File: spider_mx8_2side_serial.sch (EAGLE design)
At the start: 7 parts, among them J1 AVR_SPI_PRG_6NS

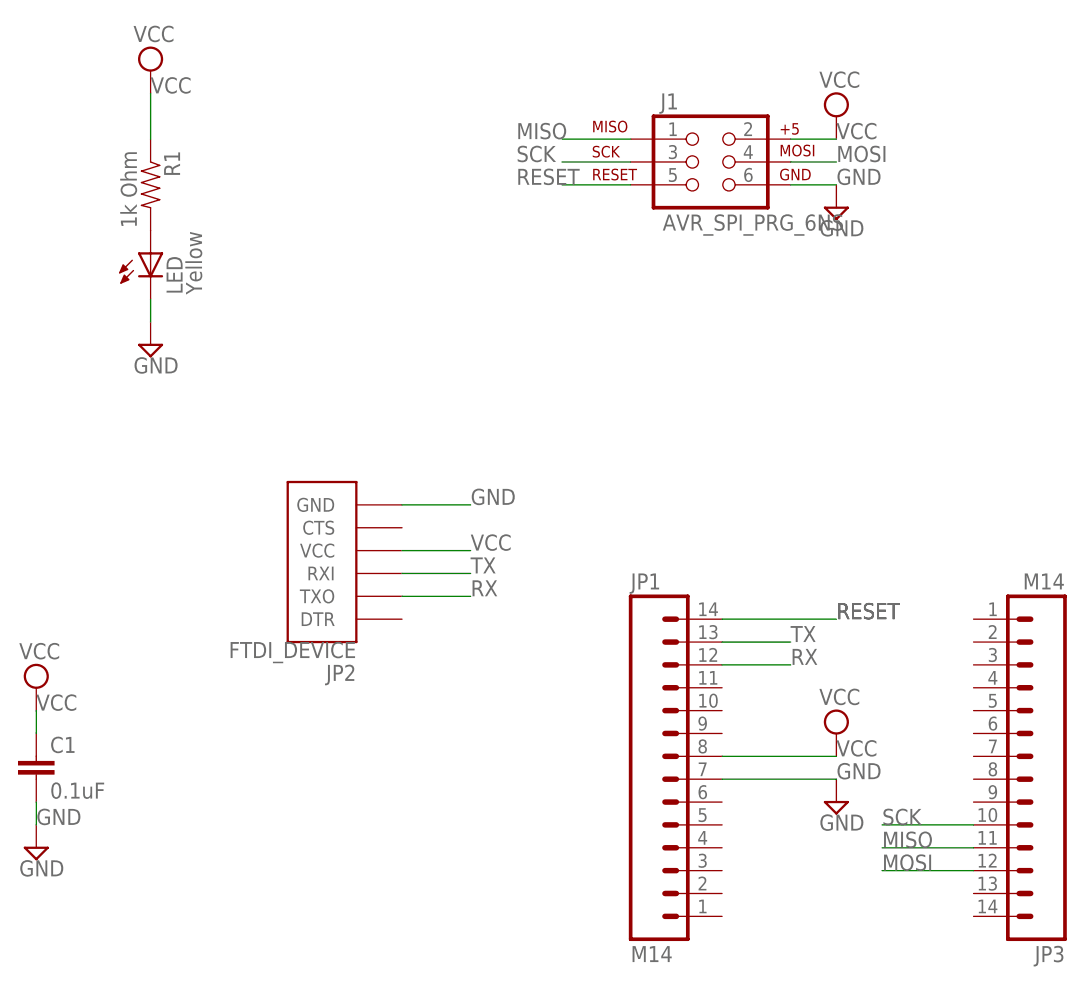
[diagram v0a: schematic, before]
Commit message: added power jumper to serial: mx8 spider
other tweaks include stuff with the 8LED modules
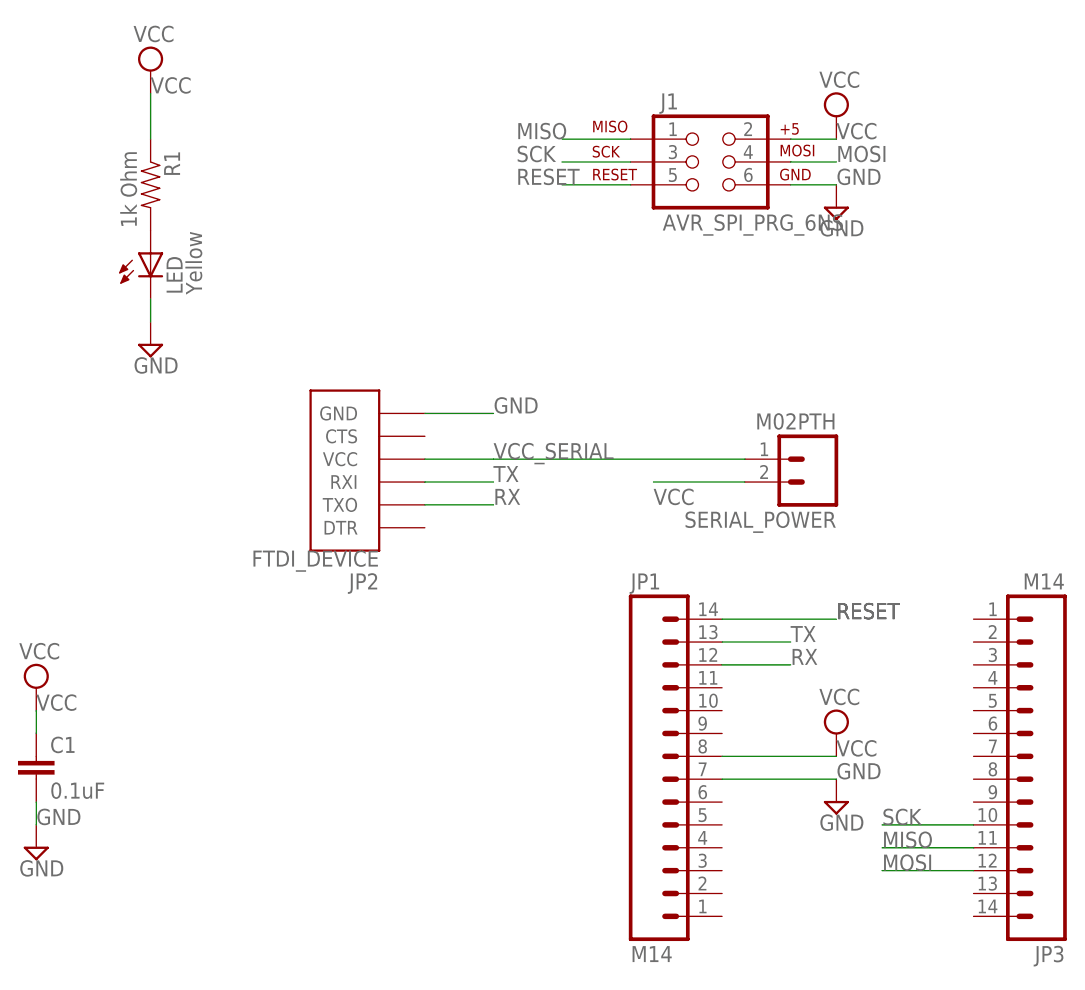
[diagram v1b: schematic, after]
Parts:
- added SERIAL_POWER: M02PTH, SparkFun-Connectors:M02PTH
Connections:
- new net VCC_SERIAL: JP2.VCC, SERIAL_POWER.1
- net VCC: now also SERIAL_POWER.2; no longer JP2.VCC
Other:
- moved on the sheet: JP2
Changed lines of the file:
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@@
 <grid distance="0.1" unitdist="inch" unit="inch" style="lines" multiple="1" display="no" altdistance="0.01" altunitdist="inch" altunit="inch"/>
 <layers>
-<layer number="1" name="Top" color="4" fill="1" visible="yes" active="no"/>
-<layer number="16" name="Bottom" color="1" fill="1" visible="yes" active="no"/>
-<layer number="17" name="Pads" color="2" fill="1" visible="yes" active="no"/>
-<layer number="18" name="Vias" color="2" fill="1" visible="yes" active="no"/>
-<layer number="19" name="Unrouted" color="6" fill="1" visible="yes" active="no"/>
-<layer number="20" name="Dimension" color="15" fill="1" visible="yes" active="no"/>
-<layer number="21" name="tPlace" color="7" fill="1" visible="yes" active="no"/>
-<layer number="22" name="bPlace" color="7" fill="1" visible="yes" active="no"/>
-<layer number="23" name="tOrigins" color="15" fill="1" visible="yes" active="no"/>
-<layer number="24" name="bOrigins" color="15" fill="1" visible="yes" active="no"/>
-<layer number="25" name="tNames" color="7" fill="1" visible="yes" active="no"/>
-<layer number="26" name="bNames" color="7" fill="1" visible="yes" active="no"/>
-<layer number="27" name="tValues" color="7" fill="1" visible="yes" active="no"/>
-<layer number="28" name="bValues" color="7" fill="1" visible="yes" active="no"/>
+<layer number="1" name="Top" color="4" fill="1" visible="no" active="no"/>
+<layer number="16" name="Bottom" color="1" fill="1" visible="no" active="no"/>
+<layer number="17" name="Pads" color="2" fill="1" visible="no" active="no"/>
+<layer number="18" name="Vias" color="2" fill="1" visible="no" active="no"/>
+<layer number="19" name="Unrouted" color="6" fill="1" visible="no" active="no"/>
+<layer number="20" name="Dimension" color="15" fill="1" visible="no" active="no"/>
+<layer number="21" name="tPlace" color="7" fill="1" visible="no" active="no"/>
+<layer number="22" name="bPlace" color="7" fill="1" visible="no" active="no"/>
+<layer number="23" name="tOrigins" color="15" fill="1" visible="no" active="no"/>
+<layer number="24" name="bOrigins" color="15" fill="1" visible="no" active="no"/>
+<layer number="25" name="tNames" color="7" fill="1" visible="no" active="no"/>
+<layer number="26" name="bNames" color="7" fill="1" visible="no" active="no"/>
+<layer number="27" name="tValues" color="7" fill="1" visible="no" active="no"/>
+<layer number="28" name="bValues" color="7" fill="1" visible="no" active="no"/>
 <layer number="29" name="tStop" color="7" fill="3" visible="no" active="no"/>
 <layer number="30" name="bStop" color="7" fill="6" visible="no" active="no"/>
@@
 <layer number="35" name="tGlue" color="7" fill="4" visible="no" active="no"/>
 <layer number="36" name="bGlue" color="7" fill="5" visible="no" active="no"/>
-<layer number="37" name="tTest" color="7" fill="1" visible="yes" active="no"/>
-<layer number="38" name="bTest" color="7" fill="1" visible="yes" active="no"/>
+<layer number="37" name="tTest" color="7" fill="1" visible="no" active="no"/>
+<layer number="38" name="bTest" color="7" fill="1" visible="no" active="no"/>
 <layer number="39" name="tKeepout" color="4" fill="11" visible="no" active="no"/>
 <layer number="40" name="bKeepout" color="1" fill="11" visible="no" active="no"/>
@@
 <layer number="44" name="Drills" color="7" fill="1" visible="no" active="no"/>
 <layer number="45" name="Holes" color="7" fill="1" visible="no" active="no"/>
-<layer number="46" name="Milling" color="3" fill="1" visible="yes" active="no"/>
-<layer number="47" name="Measures" color="7" fill="1" visible="yes" active="no"/>
-<layer number="48" name="Document" color="7" fill="1" visible="yes" active="no"/>
-<layer number="49" name="Reference" color="7" fill="1" visible="yes" active="no"/>
-<layer number="50" name="dxf" color="7" fill="1" visible="yes" active="no"/>
-<layer number="51" name="tDocu" color="7" fill="1" visible="yes" active="no"/>
-<layer number="52" name="bDocu" color="7" fill="1" visible="yes" active="no"/>
-<layer number="53" name="tGND_GNDA" color="7" fill="9" visible="yes" active="no"/>
-<layer number="54" name="bGND_GNDA" color="1" fill="9" visible="yes" active="no"/>
-<layer number="56" name="wert" color="7" fill="1" visible="yes" active="no"/>
+<layer number="46" name="Milling" color="3" fill="1" visible="no" active="no"/>
+<layer number="47" name="Measures" color="7" fill="1" visible="no" active="no"/>
+<layer number="48" name="Document" color="7" fill="1" visible="no" active="no"/>
+<layer number="49" name="Reference" color="7" fill="1" visible="no" active="no"/>
+<layer number="50" name="dxf" color="7" fill="1" visible="no" active="no"/>
+<layer number="51" name="tDocu" color="7" fill="1" visible="no" active="no"/>
+<layer number="52" name="bDocu" color="7" fill="1" visible="no" active="no"/>
+<layer number="53" name="tGND_GNDA" color="7" fill="9" visible="no" active="no"/>
+<layer number="54" name="bGND_GNDA" color="1" fill="9" visible="no" active="no"/>
+<layer number="56" name="wert" color="7" fill="1" visible="no" active="no"/>
 <layer number="91" name="Nets" color="2" fill="1" visible="yes" active="yes"/>
 <layer number="92" name="Busses" color="1" fill="1" visible="yes" active="yes"/>
@@
 <part name="JP1" library="SparkFun-Connectors" deviceset="M14" device=""/>
 <part name="JP2" library="SparkFun-Connectors" deviceset="FTDI_DEVICE" device=""/>
+<part name="SERIAL_POWER" library="SparkFun-Connectors" deviceset="M02" device="PTH"/>
 </parts>
 <sheets>
@@
 <instance part="JP3" gate="G$1" x="93.98" y="-5.08" rot="R180"/>
 <instance part="JP1" gate="G$1" x="45.72" y="-2.54"/>
-<instance part="JP2" gate="G$1" x="15.24" y="17.78" rot="R180"/>
+<instance part="JP2" gate="G$1" x="17.78" y="27.94" rot="R180"/>
+<instance part="SERIAL_POWER" gate="G$1" x="66.04" y="30.48" rot="R180"/>
 </instances>
 <busses>
@@
 </segment>
 <segment>
-<label x="27.94" y="20.32" size="1.778" layer="95"/>
-<wire x1="20.32" y1="20.32" x2="27.94" y2="20.32" width="0.1524" layer="91"/>
-<pinref part="JP2" gate="G$1" pin="VCC"/>
+<wire x1="58.42" y1="27.94" x2="48.26" y2="27.94" width="0.1524" layer="91"/>
+<label x="48.26" y="25.4" size="1.778" layer="95"/>
+<pinref part="SERIAL_POWER" gate="G$1" pin="2"/>
 </segment>
 </net>
@@
 </segment>
 <segment>
-<label x="27.94" y="25.4" size="1.778" layer="95"/>
-<wire x1="20.32" y1="25.4" x2="27.94" y2="25.4" width="0.1524" layer="91"/>
+<label x="30.48" y="35.56" size="1.778" layer="95"/>
+<wire x1="22.86" y1="35.56" x2="30.48" y2="35.56" width="0.1524" layer="91"/>
 <pinref part="JP2" gate="G$1" pin="GND"/>
 </segment>
@@
 </segment>
 <segment>
-<label x="27.94" y="15.24" size="1.778" layer="95"/>
-<wire x1="20.32" y1="15.24" x2="27.94" y2="15.24" width="0.1524" layer="91"/>
+<label x="30.48" y="25.4" size="1.778" layer="95"/>
+<wire x1="22.86" y1="25.4" x2="30.48" y2="25.4" width="0.1524" layer="91"/>
 <pinref part="JP2" gate="G$1" pin="TXO"/>
 </segment>
@@
 </segment>
 <segment>
-<label x="27.94" y="17.78" size="1.778" layer="95"/>
-<wire x1="20.32" y1="17.78" x2="27.94" y2="17.78" width="0.1524" layer="91"/>
+<label x="30.48" y="27.94" size="1.778" layer="95"/>
+<wire x1="22.86" y1="27.94" x2="30.48" y2="27.94" width="0.1524" layer="91"/>
 <pinref part="JP2" gate="G$1" pin="RXI"/>
 </segment>
 </net>
+<net name="VCC_SERIAL" class="0">
+<segment>
+<label x="30.48" y="30.48" size="1.778" layer="95"/>
+<wire x1="22.86" y1="30.48" x2="30.48" y2="30.48" width="0.1524" layer="91"/>
+<pinref part="JP2" gate="G$1" pin="VCC"/>
+</segment>
+<segment>
+<wire x1="58.42" y1="30.48" x2="30.48" y2="30.48" width="0.1524" layer="91"/>
+<pinref part="SERIAL_POWER" gate="G$1" pin="1"/>
+</segment>
+</net>
